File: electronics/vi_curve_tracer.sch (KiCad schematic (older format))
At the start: 29 parts, among them P1 CONN_01X05, P2 USB_OTG, P3 CONN_01X03, P4 CONN_01X03, U1 MCP6001, U2 pic24f08km202, U3 ft230x

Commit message: Made the schematic more closely resemble the rework performed.
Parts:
- removed R8: 100, kicad_pcb:SM_0603, symbol R
- R2, R3: value 10k -> 24k
- R4, R5: value 1k -> 2.67k
- R6, R7: value 100 -> 1k
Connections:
- wire segments 120 -> 136
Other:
- note added: "Pin 1 and 2 are reversed! Fix in the next rev."
- note added: "Use HZ_OUT_1 to set the reference\nfor the differential amplifier. May move it\naround to increase the effective range."
- note removed: "Use HZ_OUT_0 to set the reference\nfor the differential amplifier. May move it\naround to increase the effective range."
- moved on the sheet: C2, C4, C6, R2, R3, R4, R5

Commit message: Saved schematic w/ program closed
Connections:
- net labels removed: HZ_OUT_0
- wire segments 136 -> 135
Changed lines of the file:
@@
 Text GLabel 2900 3900 0    60   Output ~ 0
 LZ_OUT_0
-Text GLabel 2900 4200 0    60   Input ~ 0
-HZ_OUT_0
 Text GLabel 2900 4300 0    60   Input ~ 0
 HZ_OUT_1
@@
 	3450 1450 3450 1600
 Wire Wire Line
-	2900 4200 3150 4200
-Wire Wire Line
 	3150 4300 2900 4300

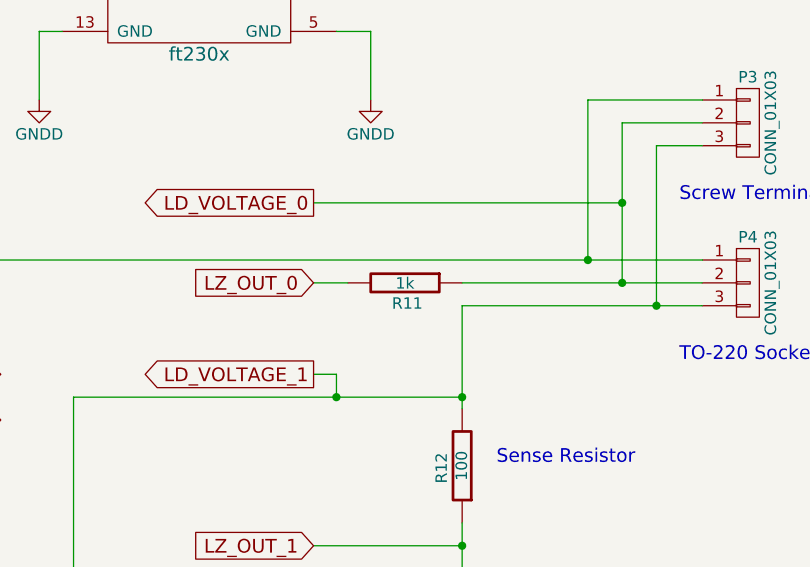
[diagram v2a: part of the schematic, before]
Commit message: Made some changes to schematic values, added PDF
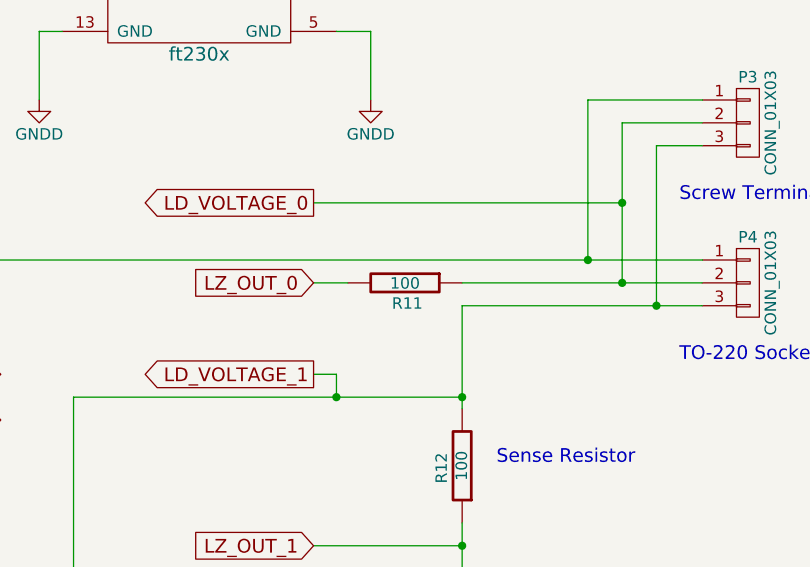
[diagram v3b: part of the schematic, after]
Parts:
- R11: value 1k -> 100
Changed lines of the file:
@@
 P 8950 3300
 F 0 "R11" V 9040 3310 50  0000 C CNN
-F 1 "1k" V 8952 3300 50  0000 C CNN
+F 1 "100" V 8952 3300 50  0000 C CNN
 F 2 "kicad_pcb:SM_0603" V 8880 3300 30  0001 C CNN
 F 3 "" H 8950 3300 30  0000 C CNN
